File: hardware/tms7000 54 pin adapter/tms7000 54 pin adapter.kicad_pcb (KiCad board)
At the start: 2 copper layers, 40.5 x 52.1 mm, 4 parts, among them J1 plcc 68, U1 DIP40 male pins

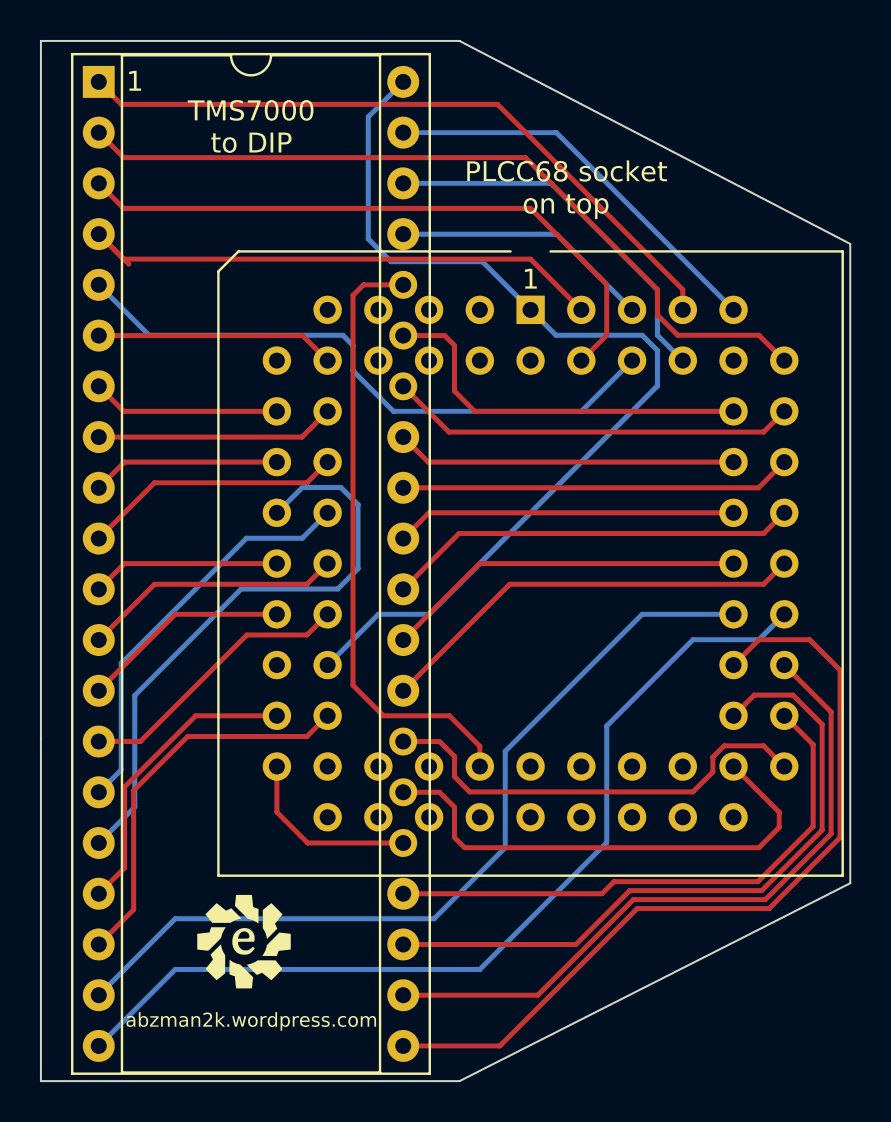
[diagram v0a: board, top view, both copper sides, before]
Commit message: fixed plcc88, added qfp60, dip54, dip64, and dip64 small pitch
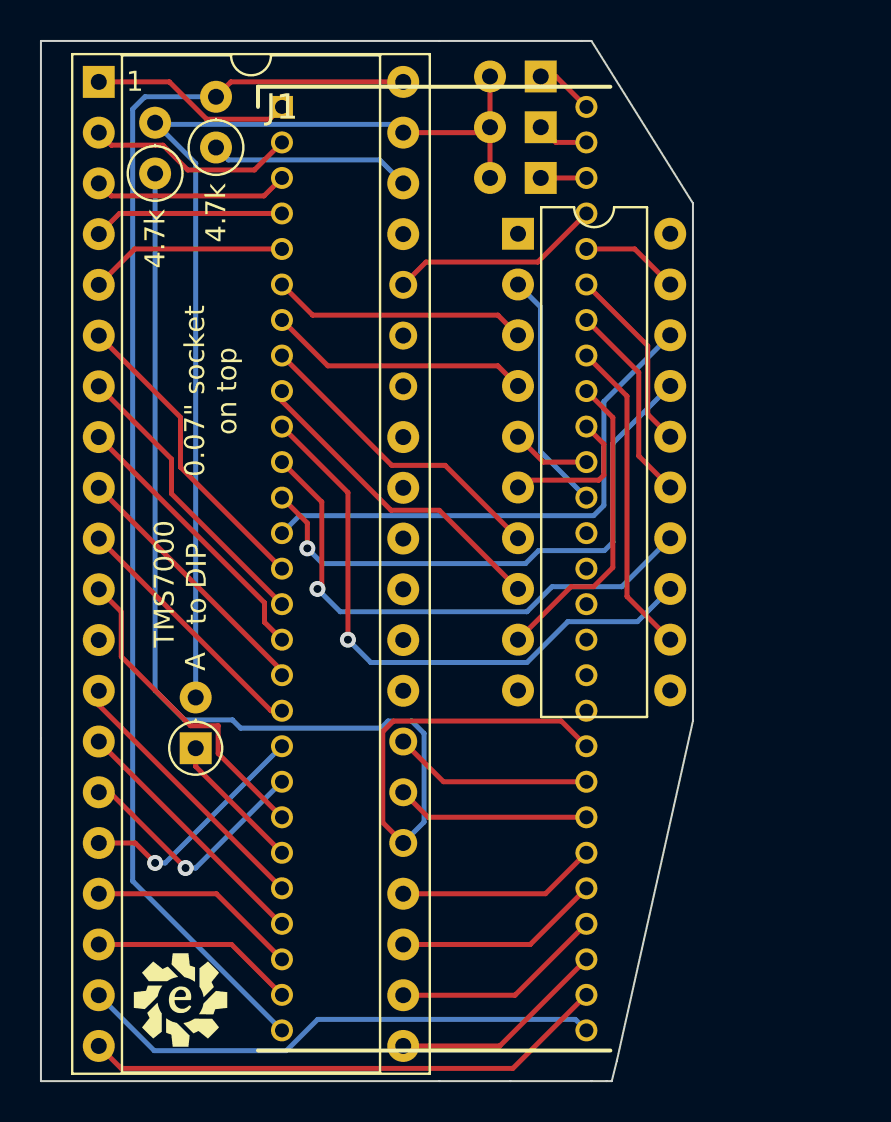
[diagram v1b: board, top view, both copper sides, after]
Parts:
- added D1: 1N4148, Diode_THT:D_DO-35_SOD27_P2.54mm_Vertical_AnodeUp, B.Cu at (142.2, 48.3)
- added D2: 1N4148, Diode_THT:D_DO-35_SOD27_P2.54mm_Vertical_AnodeUp, B.Cu at (142.2, 50.8)
- added D3: 1N4148, Diode_THT:D_DO-35_SOD27_P2.54mm_Vertical_AnodeUp, B.Cu at (142.2, 53.3)
- added D4: 1N4148, Diode_THT:D_DO-35_SOD27_P2.54mm_Vertical_AnodeUp, F.Cu at (125.0, 81.9)
- added J2: DIP20 male pins, Package_DIP:DIP-20_W7.62mm, F.Cu at (141.1, 56.1)
- added R1: 4.7k, Resistor_THT:R_Axial_DIN0207_L6.3mm_D2.5mm_P2.54mm_Vertical, F.Cu at (122.9, 53.1)
- added R2: 4.7k, Resistor_THT:R_Axial_DIN0207_L6.3mm_D2.5mm_P2.54mm_Vertical, F.Cu at (126.0, 51.8)
- J1: value plcc 68 -> dip54 narrow; footprint Package_LCC:PLCC-68_THT-Socket -> Evan's misc parts:DIP 54 1.78mm
- moved J1 16.1 mm to (129.3, 49.8)
- moved G*** 4.65 mm to (124.7, 94.7)
- moved G*** 4.31 mm to (124.2, 94.5)
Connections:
- J1 pad 1: Vss -> B5
- J1 pad 10: F7 -> E4
- J1 pad 11: A0 -> E5
- J1 pad 12: A1 -> E6
- J1 pad 13: A2 -> E7
- J1 pad 14: A3 -> A0
- J1 pad 15: A4 -> A1
- J1 pad 16: A5 -> A2
- J1 pad 17: A6 -> A3
- J1 pad 18: A7 -> A4
- J1 pad 19: /INT3 -> A5
- J1 pad 2: F0 -> B7
- J1 pad 20: /INT1 -> A6
- J1 pad 21: /RESET -> A7
- J1 pad 22: /HALT -> /CS4
- J1 pad 23: Vss -> /INT1
- J1 pad 24: XTAL2 -> /RESET
- J1 pad 25: XTAL1 -> XTAL2
- J1 pad 26: Vcc -> XTAL1
- J1 pad 27: G0 -> Vss
- J1 pad 28: unconnected-(J1-Pad28) -> D7
- J1 pad 29: G1 -> D6
- J1 pad 3: F1 -> B0
- J1 pad 30: G2 -> D5
- J1 pad 31: G3 -> D4
- J1 pad 32: G4 -> D3
- J1 pad 33: G5 -> D2
- J1 pad 34: MC -> D1
- J1 pad 35: E0 -> D0
- J1 pad 36: E1 -> Vcc
- J1 pad 37: E2 -> unconnected-(J1-Pad37)
- J1 pad 38: E3 -> unconnected-(J1-Pad38)
- J1 pad 39: E4 -> unconnected-(J1-Pad39)
- J1 pad 4: F2 -> B1
- J1 pad 40: E5 -> unconnected-(J1-Pad40)
- J1 pad 41: E6 -> unconnected-(J1-Pad41)
- J1 pad 42: E7 -> unconnected-(J1-Pad42)
- J1 pad 43: unconnected-(J1-Pad43) -> ADDR0
- J1 pad 44: D0 -> ADDR1
- J1 pad 45: D1 -> ADDR2
- J1 pad 46: D2 -> ADDR3
- J1 pad 47: D3 -> ADDR4
- J1 pad 48: D4 -> ADDR5
- J1 pad 49: D5 -> ADDR6
- J1 pad 5: F3 -> B2
- J1 pad 50: D6 -> ADDR7
- J1 pad 51: D7 -> MC
- J1 pad 52: C0 -> /CS3
- J1 pad 53: C1 -> /CS2
- J1 pad 54: C2 -> /CS1
- J1 pad 6: F4 -> E0
- J1 pad 7: F5 -> E1
- J1 pad 8: F6 -> E2
- J1 pad 9: unconnected-(J1-Pad9) -> E3
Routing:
- net Vcc: track 9.25 -> 63.4 mm
- net B6: track 20.2 -> 51.8 mm
- net E4: track 0.00 -> 30.2 mm, vias 0 -> 1
- net D5: track 41.1 -> 11.0 mm
- net B7: track 39.8 -> 10.5 mm
- net E6: track 0.00 -> 28.1 mm, vias 0 -> 1
- net E5: track 0.00 -> 26.9 mm, vias 0 -> 1
- net E7: track 0.00 -> 26.6 mm
- net B5: track 34.6 -> 10.2 mm
- net D3: track 34.1 -> 10.3 mm
- net D4: track 34.2 -> 10.7 mm
- net B0: track 31.9 -> 9.80 mm
- net C0: track 21.7 -> 0.00 mm
- net B2: track 31.1 -> 9.91 mm
- net C2: track 20.7 -> 0.00 mm
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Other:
- board size 40.5 x 52.1 mm -> 32.6 x 52.1 mm
- board text added: "0.07{dblquote} socket on top"
- board text removed: "PLCC68 socket on top"
